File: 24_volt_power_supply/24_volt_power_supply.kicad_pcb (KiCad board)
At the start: 2 copper layers, 75 x 55 mm, 16 parts, among them J1 Conn_01x02_Pin, J2 Screw_Terminal_01x02, J3 Conn_01x02_Pin, J4 Conn_01x03_Pin, K1 Relay_SPDT

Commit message: changed annotation
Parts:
- added J3: Conn_01x01_Pin, Connector_Wire:SolderWire-2.5sqmm_1x01_D2.4mm_OD3.6mm, F.Cu at (132.8, 53.4)
- added J5: Conn_01x01_Pin, Connector_Wire:SolderWire-2.5sqmm_1x01_D2.4mm_OD3.6mm, F.Cu at (109.5, 89.0)
- added J6: Conn_01x01_Pin, Connector_Wire:SolderWire-2.5sqmm_1x01_D2.4mm_OD3.6mm, F.Cu at (76.5, 76.5)
- added J7: Conn_01x01_Pin, Connector_Wire:SolderWire-2.5sqmm_1x01_D2.4mm_OD3.6mm, F.Cu at (164.5, 94.5)
- added J8: Conn_01x01_Pin, Connector_Wire:SolderWire-2.5sqmm_1x01_D2.4mm_OD3.6mm, F.Cu at (144.0, 72.0)
- J4: value Conn_01x03_Pin -> Conn_01x01_Pin; footprint Connector_Wire:SolderWire-2.5sqmm_1x03_P7.2mm_D2.4mm_OD3.6mm -> Connector_Wire:SolderWire-2.5sqmm_1x01_D2.4mm_OD3.6mm
- moved J4 28.0 mm to (122.0, 72.0)
- moved J3 2.40 mm to (76.5, 82.9)
- moved K1 2.25 mm to (133.5, 66.0)
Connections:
- K1 pad 14: Net-(J4-Pin_3) -> Net-(J8-Pin_1)
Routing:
- net AC: track 115.7 -> 53.7 mm
- net Net-(J4-Pin_1): track 30.3 -> 0.00 mm
- net Net-(J4-Pin_3): track 30.0 -> 0.00 mm

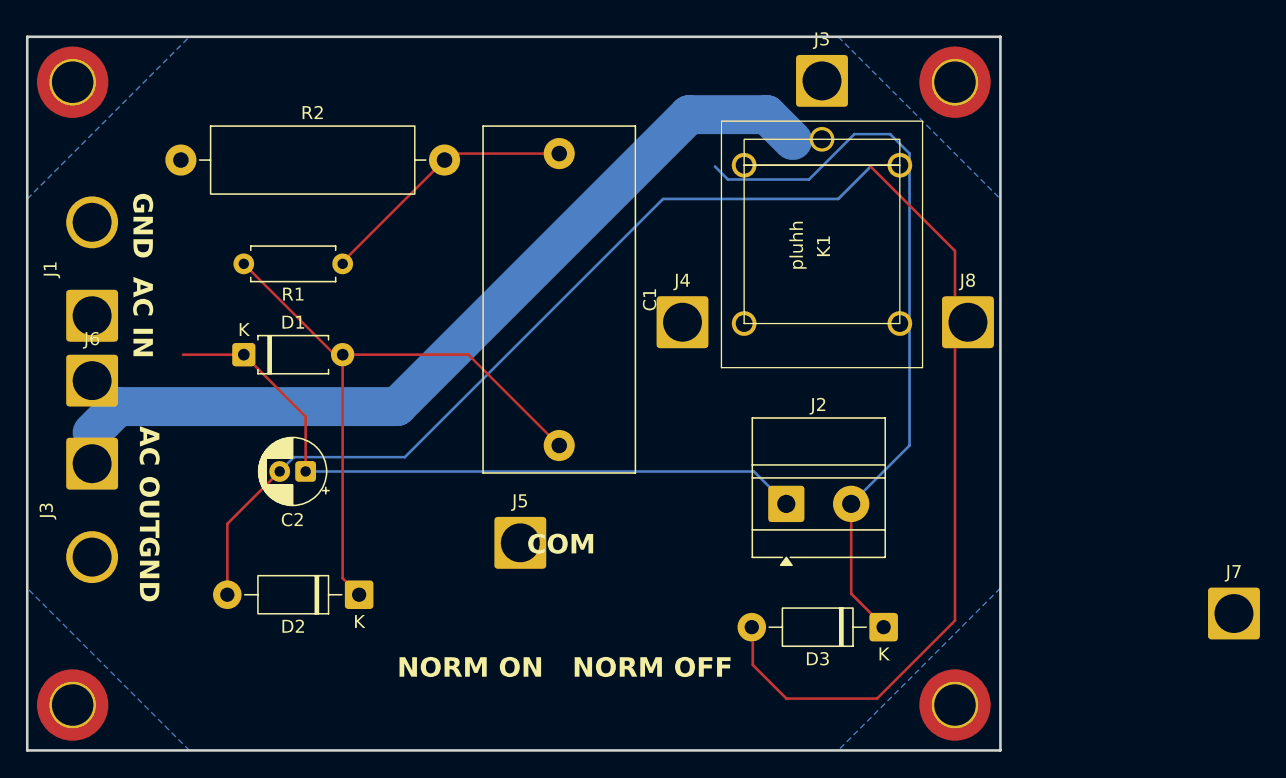
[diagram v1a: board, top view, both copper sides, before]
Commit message: first iteration of pcb with wire traces for power tranfer
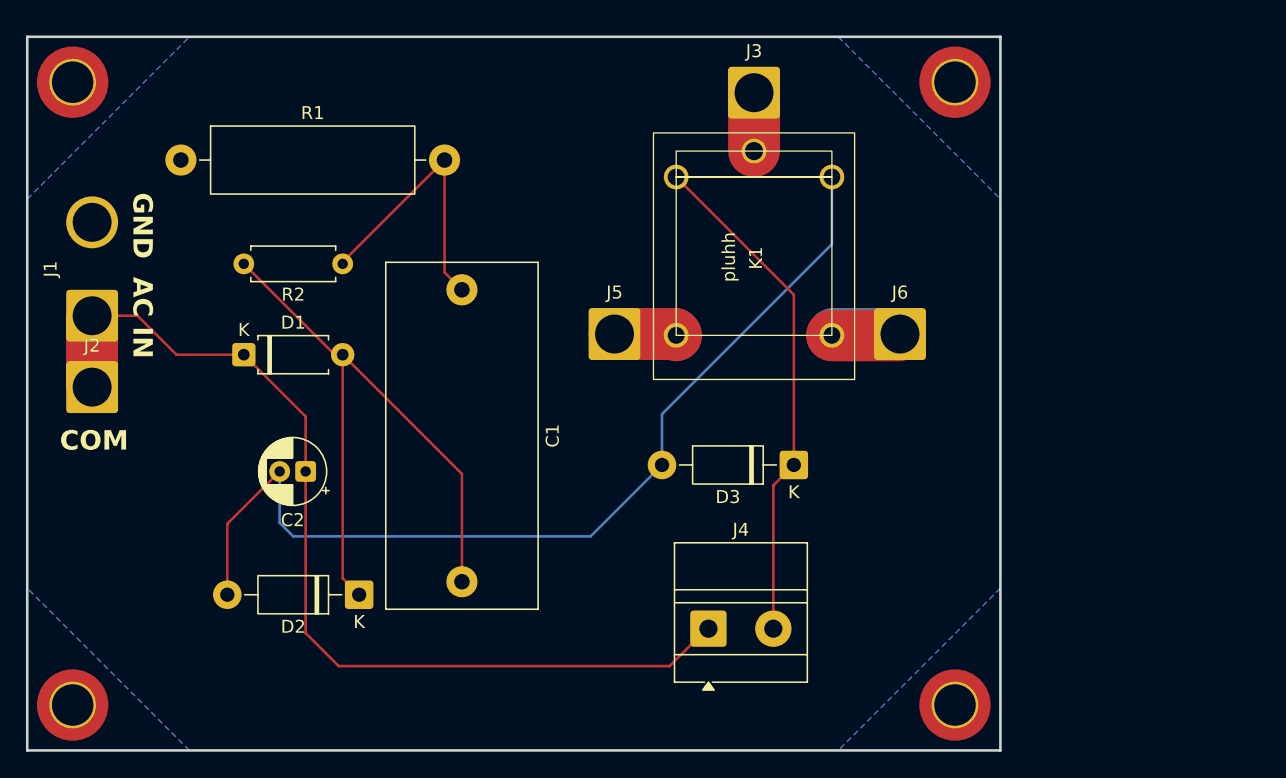
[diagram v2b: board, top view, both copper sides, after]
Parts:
- removed the J3 at (76.5, 82.9)
- removed the J5 at (109.5, 89.0)
- removed J7: Conn_01x01_Pin, Connector_Wire:SolderWire-2.5sqmm_1x01_D2.4mm_OD3.6mm
- moved D3 14.3 mm to (130.6, 83.0)
- moved C1 12.9 mm to (105.0, 69.5)
- moved J4 11.3 mm to (124.0, 95.6)
- moved J6 5.32 mm to (138.8, 72.9)
- moved K1 5.32 mm to (128.3, 66.9)
- moved J3 5.32 mm to (127.5, 54.3)
- moved J5 5.32 mm to (116.8, 72.9)
- moved J2 0.50 mm to (76.5, 77.0)
- renumbered H3 to H2, H2 to H3, J6 to J2, J2 to J4, J4 to J5, J8 to J6, R2 to R1, R1 to R2
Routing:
- net Net-(J3-Pin_1): track 65.0 -> 4.50 mm
- net Net-(D2-A): track 126.2 -> 74.9 mm
- net AC: track 53.7 -> 75.2 mm
- net Net-(D3-K): track 56.9 -> 39.2 mm
- net Net-(J6-Pin_1): track 0.00 -> 10.6 mm
- net Net-(J5-Pin_1): track 0.00 -> 9.58 mm
- net Net-(D1-A): track 49.1 -> 50.9 mm
- net Net-(C1-Pad1): track 20.3 -> 21.8 mm
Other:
- board text removed: "AC OUT"
- board text removed: "NORM OFF"
- board text removed: "NORM ON"

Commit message: flipped relay for better packaging
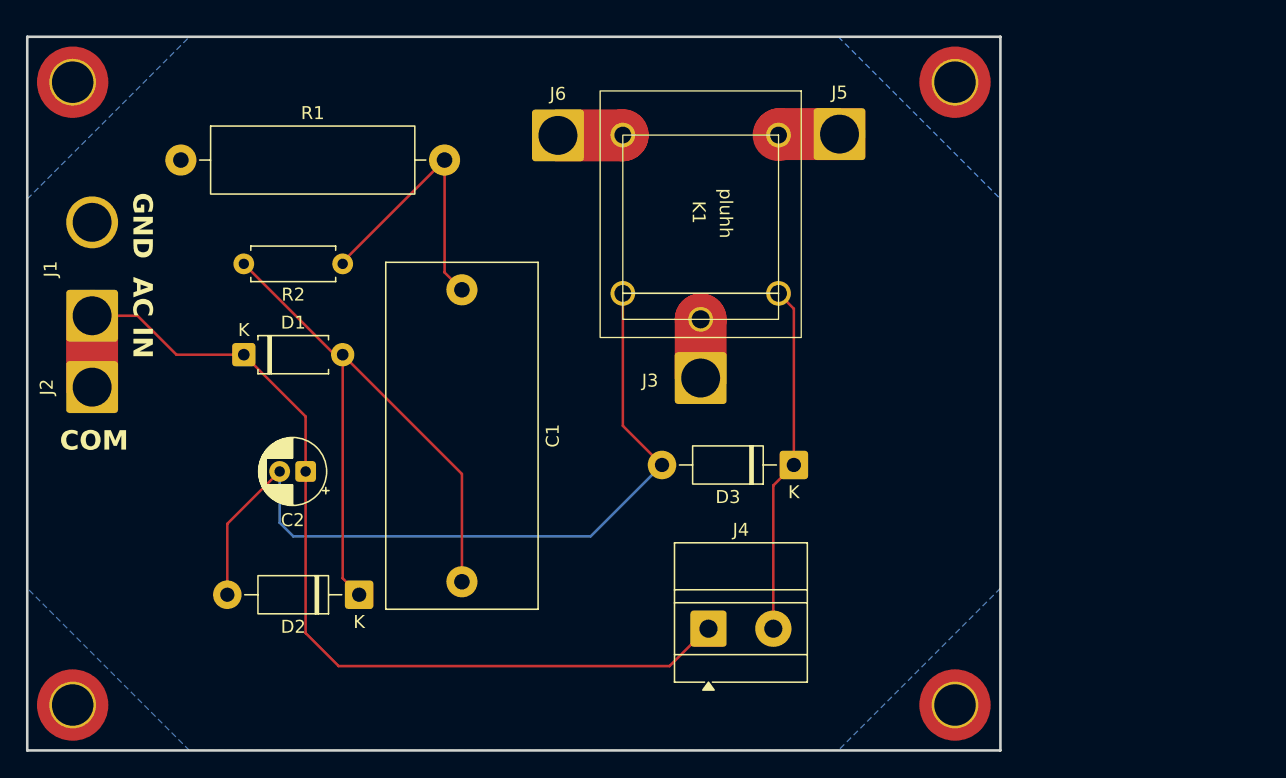
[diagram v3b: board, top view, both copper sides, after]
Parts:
- moved J6 30.5 mm to (112.4, 57.6)
- moved J5 23.2 mm to (134.1, 57.5)
- moved J3 22.4 mm to (123.4, 76.3)
- moved K1 6.48 mm to (122.7, 63.7), turned to -90 degrees
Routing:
- net Net-(D2-A): track 74.9 -> 61.8 mm
- net Net-(D3-K): track 39.2 -> 27.0 mm
- net Net-(J6-Pin_1): track 10.6 -> 5.01 mm
- net Net-(J5-Pin_1): track 9.58 -> 4.73 mm
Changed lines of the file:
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@@
 		(tags "connector wire 2.5sqmm")
 		(property "Reference" "J2"
-			(at 0 -3.2 0)
+			(at -3.5 0 90)
 			(layer "F.SilkS")
 			(effects
@@
 	(footprint "J1071CS24VDC.36:Relay_Cit_J1071CS24VDC.36"
 		(layer "F.Cu")
-		(at 128.262938 66.909667 90)
+		(at 122.651255 63.675855 -90)
 		(property "Reference" "K1"
-			(at -0.15 -0.6 90)
+			(at -0.15 -0.6 270)
 			(unlocked yes)
 			(layer "F.SilkS")
@@
 		)
 		(property "Value" "Relay_SPDT"
-			(at 0.4 3 90)
+			(at 0.4 3 270)
 			(unlocked yes)
 			(layer "F.Fab")
@@
 		)
 		(property "Datasheet" "https://www.citrelay.com/wp-content/uploads/2025/05/Relay-J107.pdf"
-			(at 0 0 90)
+			(at 0 0 270)
 			(unlocked yes)
 			(layer "F.Fab")
@@
 		)
 		(property "Description" "Relay SPDT, monostable, EN50005"
-			(at 0 0 90)
+			(at 0 0 270)
 			(unlocked yes)
 			(layer "F.Fab")
@@
 		(attr smd)
 		(fp_rect
-			(start -9.5 -8.5)
-			(end 9.5 7)
+			(start -6.1 -6.75)
+			(end 6.1 5.25)
 			(stroke
 				(width 0.1)
@@
 		)
 		(fp_rect
-			(start -6.1 -6.75)
-			(end 6.1 5.25)
+			(start -9.5 -8.5)
+			(end 9.5 7)
 			(stroke
 				(width 0.1)
@@
 		)
 		(fp_text user "pluhh"
-			(at -2 -2.1 90)
+			(at -2 -2.1 270)
 			(unlocked yes)
 			(layer "F.SilkS")
@@
 		)
 		(fp_text user "${REFERENCE}"
-			(at -0.1 1.4 90)
+			(at -0.1 1.4 270)
 			(unlocked yes)
 			(layer "F.Fab")
@@
 		)
 		(pad "11" thru_hole circle
-			(at 8.1 -0.75 90)
+			(at 8.1 -0.75 270)
 			(size 1.905 1.905)
 			(drill 1.4)
@@
 		)
 		(pad "12" thru_hole circle
-			(at -6.1 -6.75 90)
+			(at -6.1 -6.75 270)
 			(size 1.905 1.905)
 			(drill 1.3)
@@
 		)
 		(pad "14" thru_hole circle
-			(at -6.1 5.25 90)
+			(at -6.1 5.25 270)
 			(size 1.905 1.905)
 			(drill 1.3)
@@
 		)
 		(pad "A1" thru_hole circle
-			(at 6.1 -6.75 90)
+			(at 6.1 -6.75 270)
 			(size 1.905 1.905)
 			(drill 1.3)
@@
 		)
 		(pad "A2" thru_hole circle
-			(at 6.1 5.25 90)
+			(at 6.1 5.25 270)
 			(size 1.905 1.905)
 			(drill 1.3)
@@
 	(footprint "Connector_Wire:SolderWire-2.5sqmm_1x01_D2.4mm_OD3.6mm"
 		(layer "F.Cu")
-		(at 127.512938 54.309667)
+		(at 123.4 76.3)
 		(descr "Soldered wire connection, for a single 2.5 mm² wire, basic insulation, conductor diameter 2.4mm, outer diameter 3.6mm, size source Multi-Contact FLEXI-E 2.5 (https://www.staubli.com/content/dam/ecs/catalogs-brochures/TM/CAB-Main-11014119-en.pdf#page=9), bend radius 3 times outer diameter, generated with kicad-footprint-generator")
 		(tags "connector wire 2.5sqmm")
 		(property "Reference" "J3"
-			(at 0 -3.2 0)
+			(at -3.9 0.2 0)
 			(layer "F.SilkS")
 			(effects
@@
 	(footprint "Connector_Wire:SolderWire-2.5sqmm_1x01_D2.4mm_OD3.6mm"
 		(layer "F.Cu")
-		(at 138.762938 72.909667)
+		(at 112.4 57.6)
 		(descr "Soldered wire connection, for a single 2.5 mm² wire, basic insulation, conductor diameter 2.4mm, outer diameter 3.6mm, size source Multi-Contact FLEXI-E 2.5 (https://www.staubli.com/content/dam/ecs/catalogs-brochures/TM/CAB-Main-11014119-en.pdf#page=9), bend radius 3 times outer diameter, generated with kicad-footprint-generator")
 		(tags "connector wire 2.5sqmm")
@@
 	(footprint "Connector_Wire:SolderWire-2.5sqmm_1x01_D2.4mm_OD3.6mm"
 		(layer "F.Cu")
-		(at 116.762938 72.909667)
+		(at 134.1 57.5)
 		(descr "Soldered wire connection, for a single 2.5 mm² wire, basic insulation, conductor diameter 2.4mm, outer diameter 3.6mm, size source Multi-Contact FLEXI-E 2.5 (https://www.staubli.com/content/dam/ecs/catalogs-brochures/TM/CAB-Main-11014119-en.pdf#page=9), bend radius 3 times outer diameter, generated with kicad-footprint-generator")
 		(tags "connector wire 2.5sqmm")
@@
 	)
 	(segment
-		(start 86.92 93)
-		(end 86.92 87.535113)
+		(start 117.401255 79.981255)
+		(end 120.42 83)
 		(width 0.2)
 		(layer "F.Cu")
@@
 	)
 	(segment
-		(start 86.92 87.535113)
-		(end 90.955113 83.5)
+		(start 86.92 93)
+		(end 86.92 87.535113)
 		(width 0.2)
 		(layer "F.Cu")
@@
 	)
 	(segment
-		(start 133.512938 60.809667)
-		(end 133.512938 65.987062)
+		(start 117.401255 69.775855)
+		(end 117.401255 79.981255)
 		(width 0.2)
-		(layer "B.Cu")
-		(net 4)
-	)
-	(segment
-		(start 114.92 88.5)
-		(end 120.42 83)
-		(width 0.2)
-		(layer "B.Cu")
+		(layer "F.Cu")
 		(net 4)
 	)
 	(segment
-		(start 133.512938 65.987062)
-		(end 120.42 79.08)
+		(start 86.92 87.535113)
+		(end 90.955113 83.5)
 		(width 0.2)
-		(layer "B.Cu")
+		(layer "F.Cu")
 		(net 4)
 	)
 	(segment
-		(start 120.42 79.08)
+		(start 114.92 88.5)
 		(end 120.42 83)
 		(width 0.2)
@@
 	)
 	(segment
-		(start 121.512938 60.809667)
-		(end 130.58 69.876729)
+		(start 130.58 83)
+		(end 130.58 70.9546)
 		(width 0.2)
 		(layer "F.Cu")
@@
 	)
 	(segment
-		(start 129 84.58)
-		(end 130.58 83)
+		(start 130.58 70.9546)
+		(end 129.401255 69.775855)
 		(width 0.2)
 		(layer "F.Cu")
@@
 	)
 	(segment
-		(start 130.58 69.876729)
+		(start 129 84.58)
 		(end 130.58 83)
 		(width 0.2)
@@
 	)
 	(segment
-		(start 127.512938 58.809667)
-		(end 127.512938 54.309667)
+		(start 123.4 76.3)
+		(end 123.4 71.77711)
 		(width 4)
 		(layer "F.Cu")
@@
 	)
 	(segment
-		(start 133.512938 73.009667)
-		(end 138.662938 73.009667)
+		(start 123.4 71.77711)
+		(end 123.401255 71.775855)
 		(width 4)
 		(layer "F.Cu")
-		(net 8)
+		(net 7)
 	)
 	(segment
-		(start 138.662938 73.009667)
-		(end 138.762938 72.909667)
-		(width 0.2)
+		(start 117.37711 57.6)
+		(end 117.401255 57.575855)
+		(width 4)
 		(layer "F.Cu")
 		(net 8)
 	)
 	(segment
-		(start 138.762938 72.909667)
-		(end 133.612938 72.909667)
+		(start 112.4 57.6)
+		(end 117.37711 57.6)
 		(width 4)
-		(layer "B.Cu")
-		(net 8)
-	)
-	(segment
-		(start 133.612938 72.909667)
-		(end 133.512938 73.009667)
-		(width 0.2)
-		(layer "B.Cu")
+		(layer "F.Cu")
 		(net 8)
 	)
 	(segment
-		(start 116.762938 72.909667)
-		(end 121.412938 72.909667)
+		(start 129.47711 57.5)
+		(end 129.401255 57.575855)
 		(width 4)
 		(layer "F.Cu")
@@
 	)
 	(segment
-		(start 121.412938 72.909667)
-		(end 121.512938 73.009667)
+		(start 134.1 57.5)
+		(end 129.47711 57.5)
 		(width 4)
 		(layer "F.Cu")
 		(net 9)
 	)
-	(segment
-		(start 121.412938 72.909667)
-		(end 121.512938 73.009667)
-		(width 0.2)
-		(layer "B.Cu")
-		(net 9)
-	)
-	(segment
-		(start 116.762938 72.909667)
-		(end 121.412938 72.909667)
-		(width 4)
-		(layer "B.Cu")
-		(net 9)
-	)

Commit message: added rules to remove filled zone under high voltage connections
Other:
- board text added: "AC OUT"
- board text added: "NORM OFF"
- board text added: "NORM ON"
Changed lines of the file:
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@@
+		)
+	)
+	(gr_text "AC\nOUT"
+		(at 128.5 78.5 0)
+		(layer "F.SilkS")
+		(effects
+			(font
+				(size 1.5 1.5)
+				(thickness 0.3)
+				(bold yes)
+			)
+			(justify bottom)
 		)
 	)
@@
 		)
 	)
+	(gr_text "NORM\nOFF"
+		(at 111.5 64.5 0)
+		(layer "F.SilkS")
+		(effects
+			(font
+				(size 1.5 1.5)
+				(thickness 0.3)
+				(bold yes)
+			)
+			(justify bottom)
+		)
+	)
 	(gr_text "COM"
 		(at 74 82 0)
@@
 		)
 	)
+	(gr_text "NORM\nON"
+		(at 135 64.5 0)
+		(layer "F.SilkS")
+		(effects
+			(font
+				(size 1.5 1.5)
+				(thickness 0.3)
+				(bold yes)
+			)
+			(justify bottom)
+		)
+	)
 	(segment
 		(start 88.19 67.5)
@@
 			)
 		)
+	)
+	(zone
+		(net 0)
+		(net_name "")
+		(layer "B.Cu")
+		(hatch edge 0.5)
+		(connect_pads
+			(clearance 0)
+		)
+		(min_thickness 0.25)
+		(filled_areas_thickness no)
+		(keepout
+			(tracks allowed)
+			(vias allowed)
+			(pads allowed)
+			(copperpour not_allowed)
+			(footprints allowed)
+		)
+		(placement
+			(enabled no)
+			(sheetname "/")
+		)
+		(fill
+			(thermal_gap 0.5)
+			(thermal_bridge_width 0.5)
+		)
+		(polygon
+			(pts
+				(xy 132.1 55.1) (xy 128.95 56.2) (xy 128.95 58.95) (xy 132.05 59.95)
+			)
+		)
+	)
+	(zone
+		(net 0)
+		(net_name "")
+		(layer "B.Cu")
+		(hatch edge 0.5)
+		(connect_pads
+			(clearance 0)
+		)
+		(min_thickness 0.25)
+		(filled_areas_thickness no)
+		(keepout
+			(tracks allowed)
+			(vias allowed)
+			(pads allowed)
+			(copperpour not_allowed)
+			(footprints allowed)
+		)
+		(placement
+			(enabled no)
+			(sheetname "/")
+		)
+		(fill
+			(thermal_gap 0.5)
+			(thermal_bridge_width 0.5)
+		)
+		(polygon
+			(pts
+				(xy 74 69) (xy 79 69) (xy 79 79.5) (xy 74 79.5)
+			)
+		)
+	)
+	(zone
+		(net 0)
+		(net_name "")
+		(layer "B.Cu")
+		(hatch edge 0.5)
+		(connect_pads
+			(clearance 0)
+		)
+		(min_thickness 0.25)
+		(filled_areas_thickness no)
+		(keepout
+			(tracks allowed)
+			(vias allowed)
+			(pads allowed)
+			(copperpour not_allowed)
+			(footprints allowed)
+		)
+		(placement
+			(enabled no)
+			(sheetname "/")
+		)
+		(fill
+			(thermal_gap 0.5)
+			(thermal_bridge_width 0.5)
+		)
+		(polygon
+			(pts
+				(xy 114.3 55.1) (xy 117.7 56.15) (xy 117.7 59) (xy 114.3 60.1)
+			)
+		)
+	)
+	(zone
+		(net 0)
+		(net_name "")
+		(layer "B.Cu")
+		(hatch edge 0.5)
+		(connect_pads
+			(clearance 0)
+		)
+		(min_thickness 0.25)
+		(filled_areas_thickness no)
+		(keepout
+			(tracks allowed)
+			(vias allowed)
+			(pads allowed)
+			(copperpour not_allowed)
+			(footprints allowed)
+		)
+		(placement
+			(enabled no)
+			(sheetname "/")
+		)
+		(fill
+			(thermal_gap 0.5)
+			(thermal_bridge_width 0.5)
+		)
+		(polygon
+			(pts
+				(xy 120.9 74.4) (xy 122 71.45) (xy 124.85 71.45) (xy 125.6 74.45)
+			)
+		)
